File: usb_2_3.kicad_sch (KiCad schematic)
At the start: 21 parts, among them J4 USB3_A_Stacked, J91 USB3_A_Stacked, J92 USB_A_Stacked, U89 D3V3XA4B10LP, U90 D3V3XA4B10LP, U91 D3V3XA4B10LP

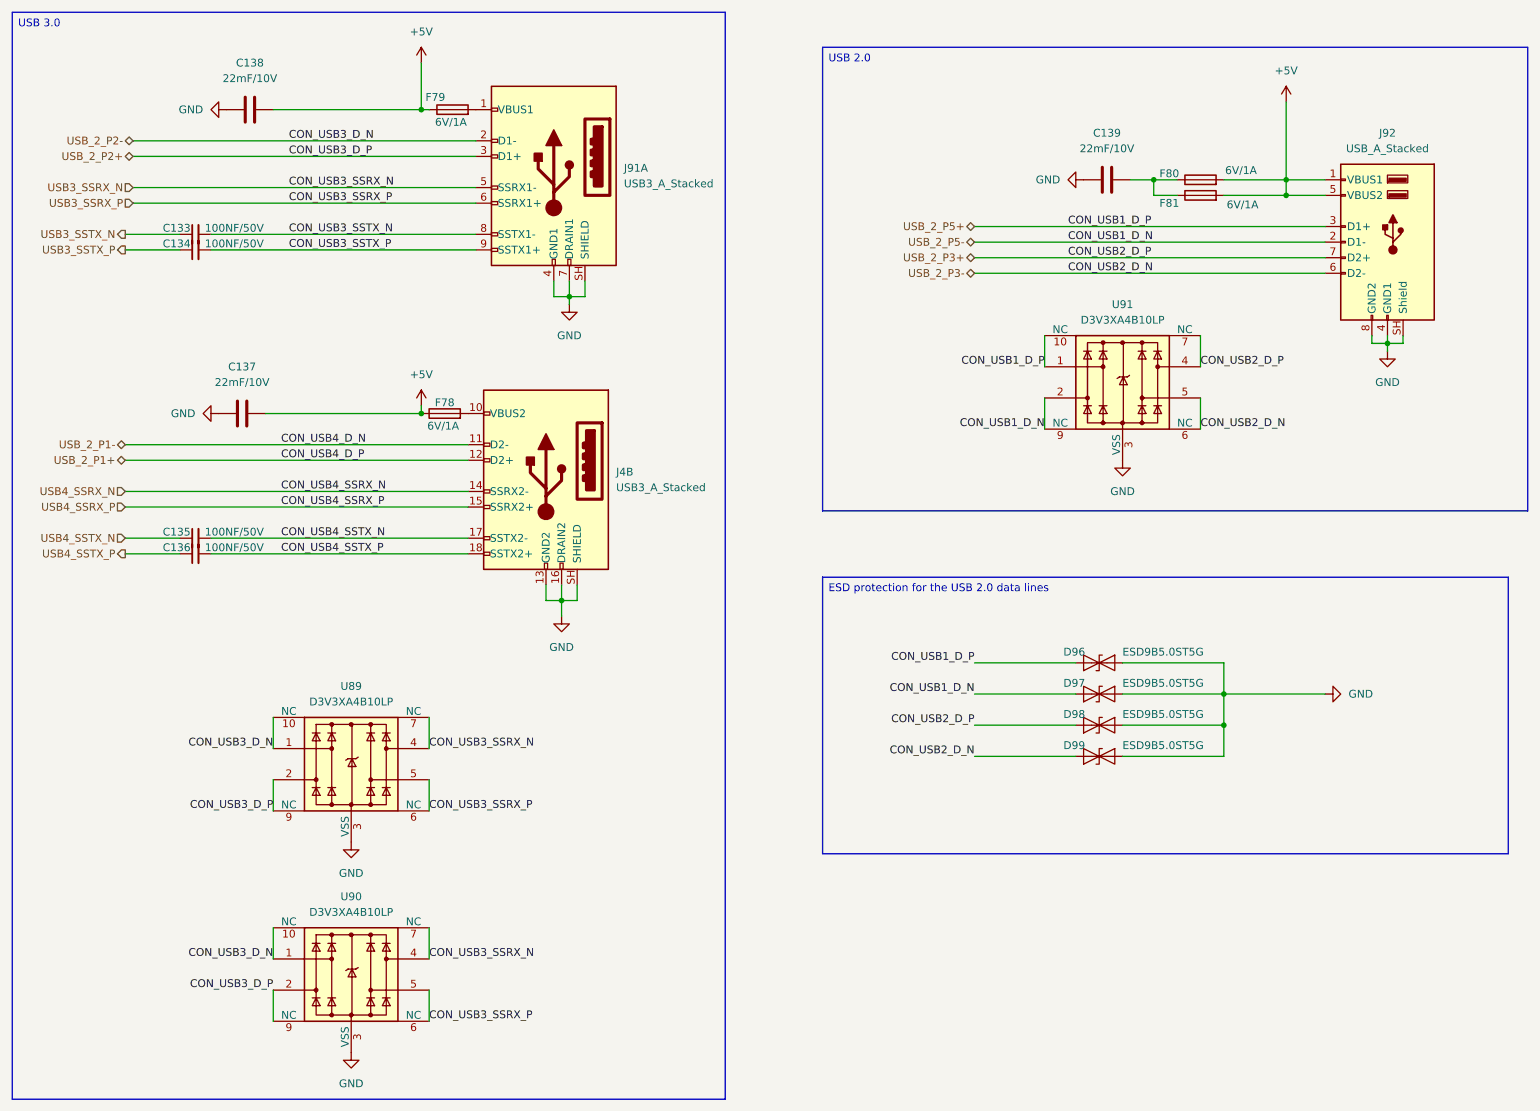
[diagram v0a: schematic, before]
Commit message: USB designators restored
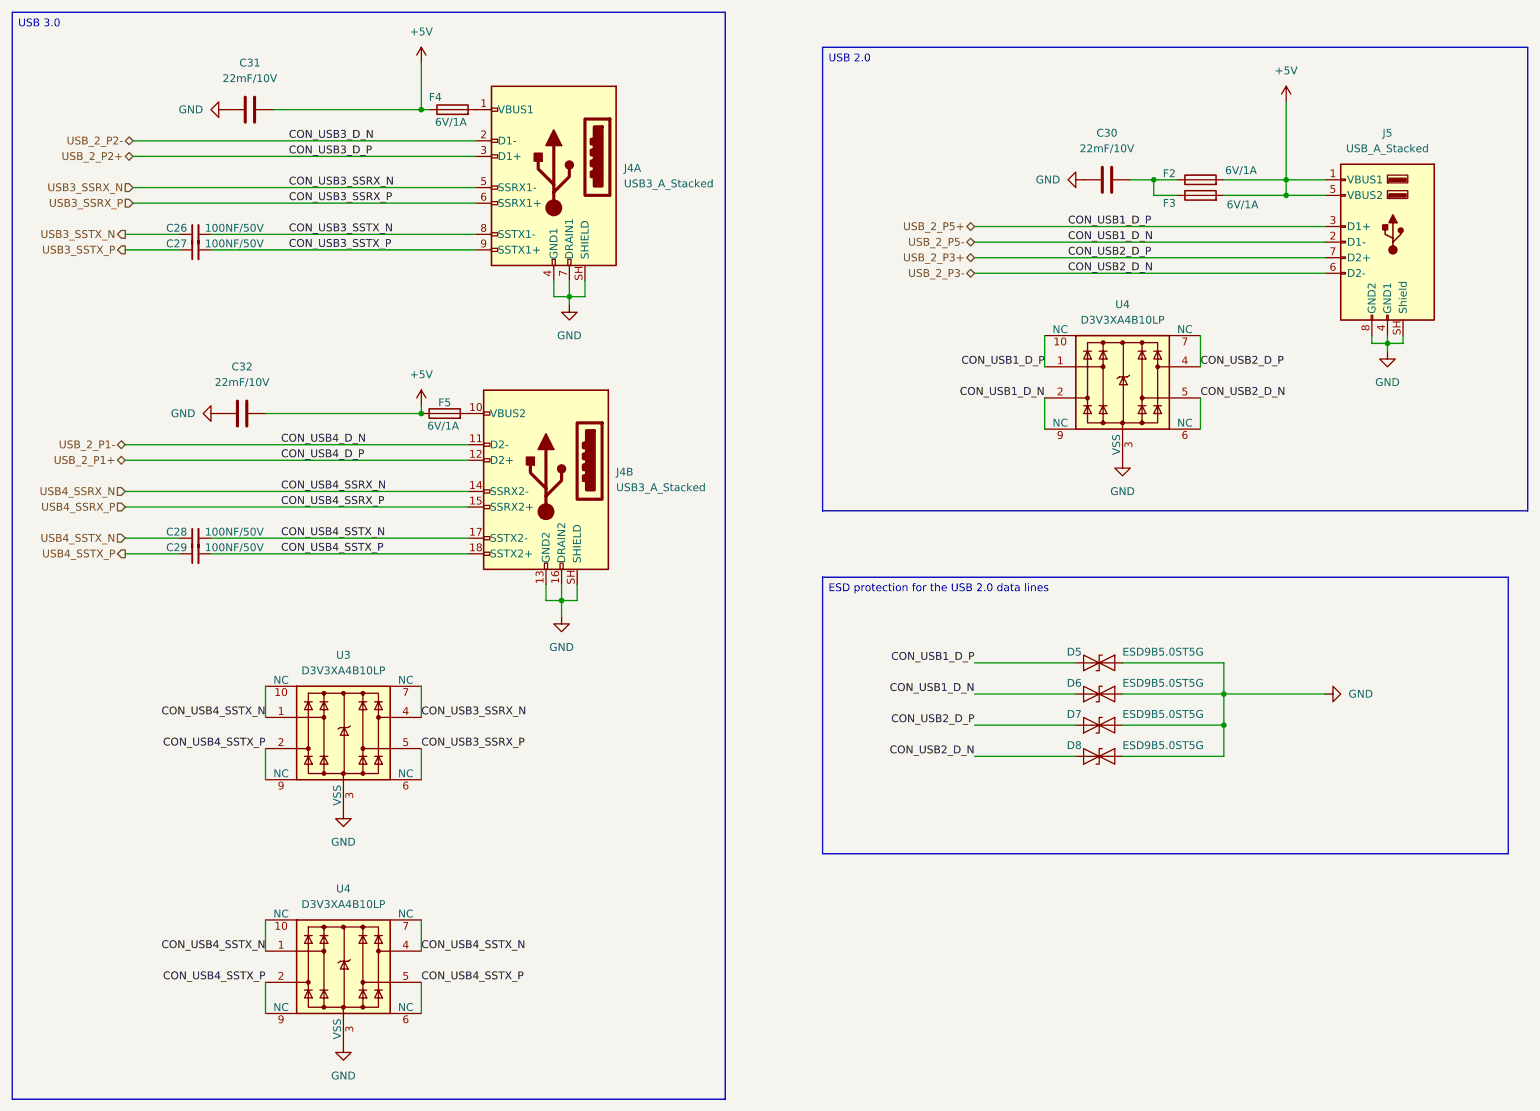
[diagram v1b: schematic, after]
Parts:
- renumbered C133 to C26, C134 to C27, C135 to C28, C136 to C29, C139 to C30, C138 to C31, C137 to C32, D96 to D5, D97 to D6, D98 to D7, D99 to D8, F80 to F2, F81 to F3, F79 to F4, F78 to F5, J91 to J4, J92 to J5, U90 to U3, U89 to U4, U91 to U4
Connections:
- net CON_USB4_SSTX_N: now also U3.1, U3.10 (NC), U4.1, U4.10 (NC), U4.4, U4.7 (NC)
- net CON_USB4_SSTX_P: now also U3.2, U3.9 (NC), U4.2, U4.5, U4.6 (NC), U4.9 (NC)
- net USB3_SSRX_N: no longer U4.4, U4.7 (NC)
- net USB3_SSRX_P: no longer U4.5, U4.6 (NC)
- net USB_2_P2+: no longer U3.2, U3.9 (NC), U4.2, U4.9 (NC)
- net USB_2_P2-: no longer U3.1, U3.10 (NC), U4.1, U4.10 (NC)
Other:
- moved on the sheet: U3, U4

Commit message: Designators in GPIO restored
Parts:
- renumbered U4 to U5
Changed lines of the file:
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@@
 		(dnp no)
 		(fields_autoplaced yes)
-		(property "Reference" "U4"
+		(property "Reference" "U5"
 			(at 67.31 156.21 0)
 			(show_name no)
@@
 			(project "Carrier_Board"
 				(path "/e768274e-12f3-4f83-96f6-abb7638e0bc1/f6805346-90aa-47cf-a186-fe5806ffb5a5"
-					(reference "U4")
+					(reference "U5")
 					(unit 1)
 				)
